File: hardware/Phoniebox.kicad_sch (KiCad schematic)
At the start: 11 parts, among them J1 GPIO, J2 Screw_Terminal_01x08, J3 Screw_Terminal_01x08, J4 Screw_Terminal_01x08, J5 Conn_02x02_Odd_Even, J7 USB_C_Receptacle_USB2.0, J8 Conn_02x04_Odd_Even, U4 CAT24C32

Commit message: Smaller high value caps. Standard R/C footprints instead of hand solder.
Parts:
- R1, R2, R30: footprint Resistor_SMD:R_0603_1608Metric_Pad0.98x0.95mm_HandSolder -> Resistor_SMD:R_0603_1608Metric

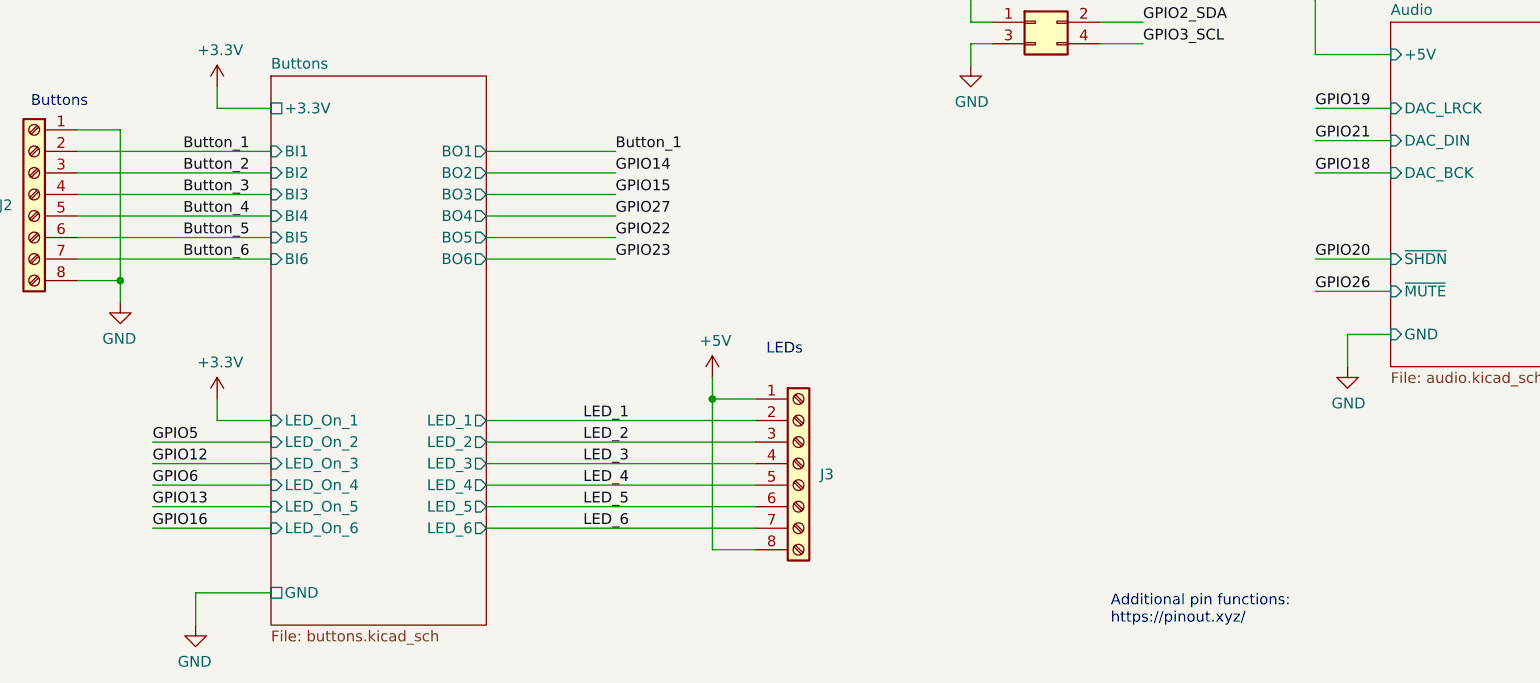
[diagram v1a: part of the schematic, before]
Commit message: Move a lot of parts. Switch audio l/r (only in schematic). Next step: Apply in PCB.
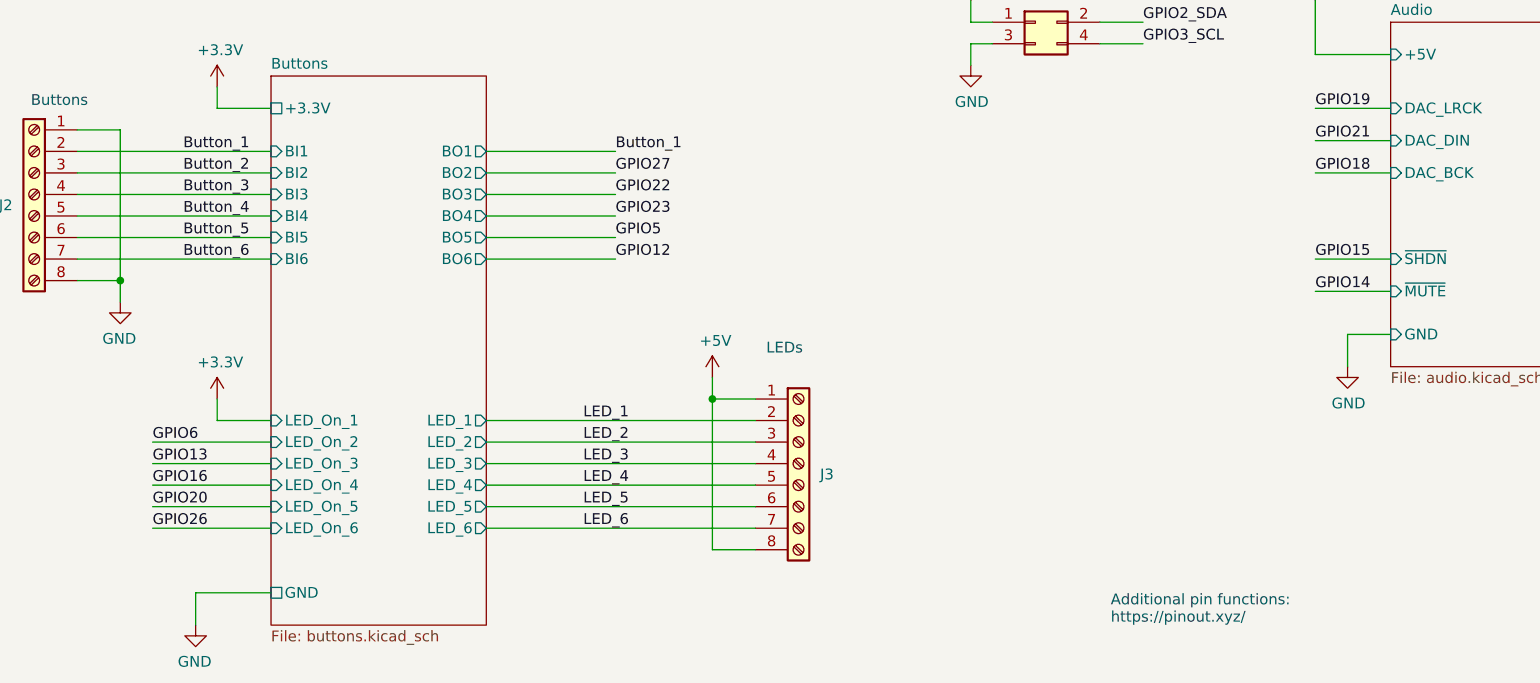
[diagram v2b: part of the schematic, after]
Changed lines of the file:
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@@
     (effects (font (size 1.27 1.27)) (justify left bottom))
   )
-  (label "GPIO23" (at 120.65 137.16 0)
+  (label "GPIO12" (at 120.65 137.16 0)
     (effects (font (size 1.27 1.27)) (justify left bottom))
   )
@@
     (effects (font (size 1.27 1.27)) (justify left bottom))
   )
-  (label "GPIO20" (at 203.2 137.16 0)
+  (label "GPIO15" (at 203.2 137.16 0)
     (effects (font (size 1.27 1.27)) (justify left bottom))
   )
@@
     (effects (font (size 1.27 1.27)) (justify right bottom))
   )
-  (label "GPIO13" (at 66.04 166.37 0)
+  (label "GPIO20" (at 66.04 166.37 0)
     (effects (font (size 1.27 1.27)) (justify left bottom))
   )
@@
     (effects (font (size 1.27 1.27)) (justify right bottom))
   )
-  (label "GPIO16" (at 66.04 168.91 0)
+  (label "GPIO26" (at 66.04 168.91 0)
     (effects (font (size 1.27 1.27)) (justify left bottom))
   )
@@
     (effects (font (size 1.27 1.27)) (justify right bottom))
   )
-  (label "GPIO22" (at 120.65 134.62 0)
-    (effects (font (size 1.27 1.27)) (justify left bottom))
-  )
-  (label "GPIO14" (at 120.65 127 0)
-    (effects (font (size 1.27 1.27)) (justify left bottom))
-  )
-  (label "GPIO12" (at 66.04 161.29 0)
-    (effects (font (size 1.27 1.27)) (justify left bottom))
-  )
-  (label "GPIO5" (at 66.04 158.75 0)
-    (effects (font (size 1.27 1.27)) (justify left bottom))
-  )
-  (label "GPIO27" (at 120.65 132.08 0)
-    (effects (font (size 1.27 1.27)) (justify left bottom))
-  )
-  (label "GPIO6" (at 66.04 163.83 0)
-    (effects (font (size 1.27 1.27)) (justify left bottom))
-  )
-  (label "GPIO26" (at 203.2 140.97 0)
+  (label "GPIO5" (at 120.65 134.62 0)
+    (effects (font (size 1.27 1.27)) (justify left bottom))
+  )
+  (label "GPIO27" (at 120.65 127 0)
+    (effects (font (size 1.27 1.27)) (justify left bottom))
+  )
+  (label "GPIO13" (at 66.04 161.29 0)
+    (effects (font (size 1.27 1.27)) (justify left bottom))
+  )
+  (label "GPIO6" (at 66.04 158.75 0)
+    (effects (font (size 1.27 1.27)) (justify left bottom))
+  )
+  (label "GPIO23" (at 120.65 132.08 0)
+    (effects (font (size 1.27 1.27)) (justify left bottom))
+  )
+  (label "GPIO16" (at 66.04 163.83 0)
+    (effects (font (size 1.27 1.27)) (justify left bottom))
+  )
+  (label "GPIO14" (at 203.2 140.97 0)
     (effects (font (size 1.27 1.27)) (justify left bottom))
   )
@@
     (effects (font (size 1.27 1.27)) (justify left bottom))
   )
-  (label "GPIO15" (at 120.65 129.54 0)
-    (effects (font (size 1.27 1.27)) (justify left bottom))
-  )
+  (label "GPIO22" (at 120.65 129.54 0)
+    (effects (font (size 1.27 1.27)) (justify left bottom))
+  )

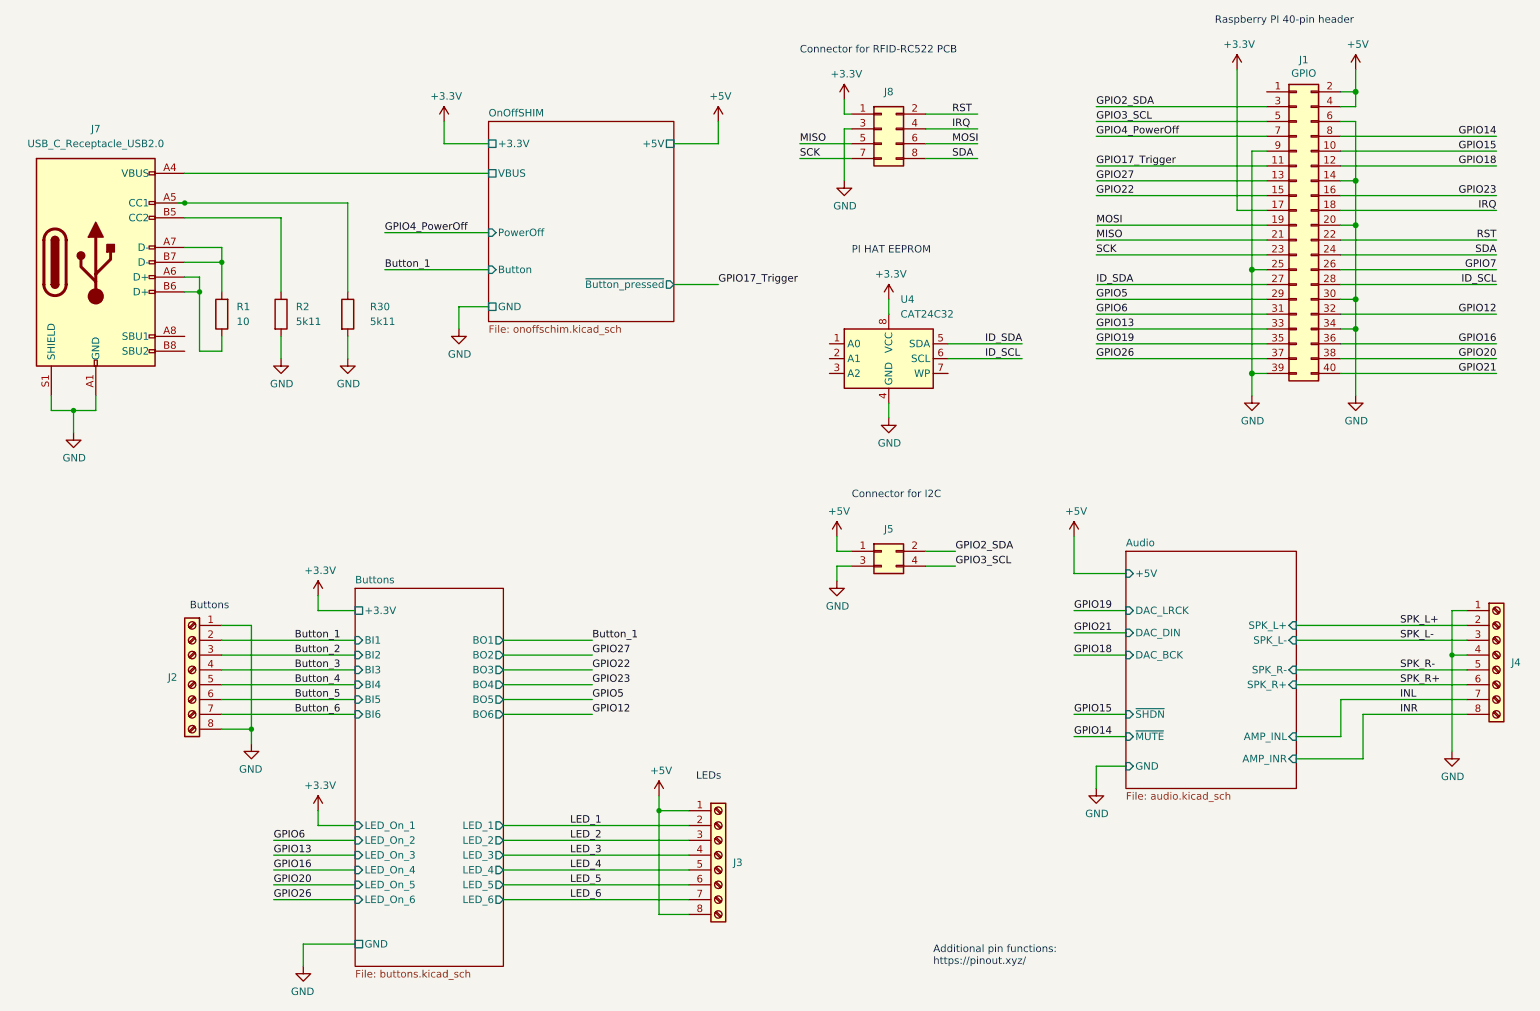
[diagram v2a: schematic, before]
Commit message: Moved DAC. Replace pin headers with single row SMD ones (compatible with RC522/display PCBs to connect).
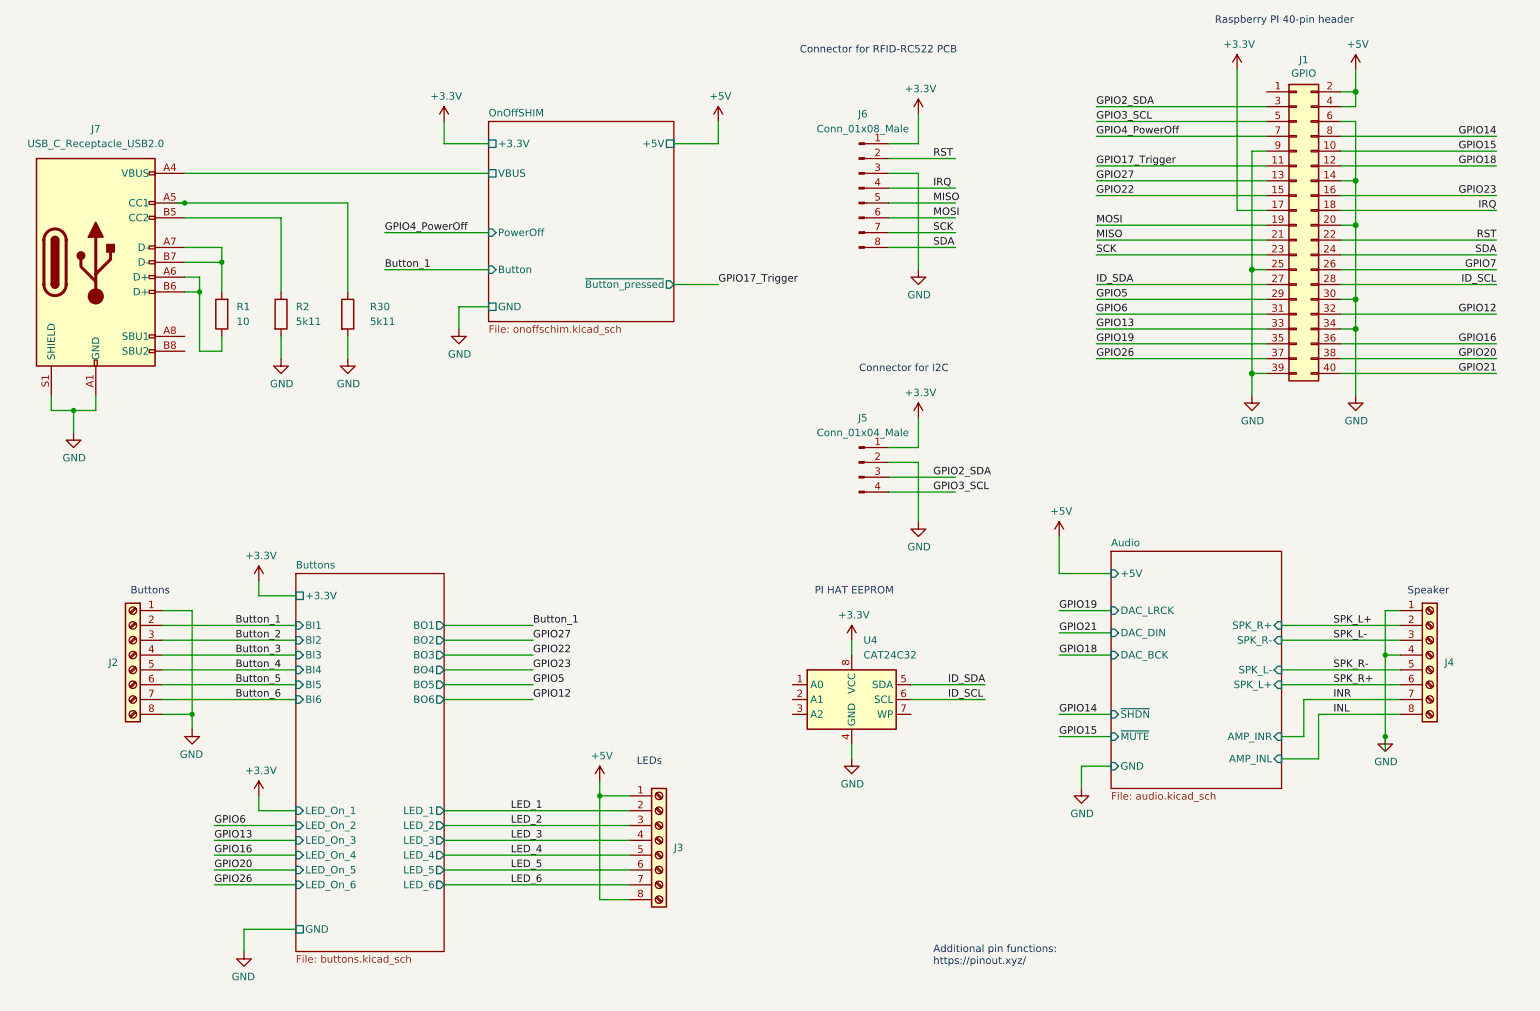
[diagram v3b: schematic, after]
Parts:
- removed J5: Conn_02x02_Odd_Even, Connector_PinHeader_2.54mm:PinHeader_2x02_P2.54mm_Vertical_SMD, symbol Connector_Generic:Conn_02x02_Odd_Even
- removed J8: Conn_02x04_Odd_Even, Connector_PinHeader_2.54mm:PinHeader_2x04_P2.54mm_Vertical_SMD, symbol Connector_Generic:Conn_02x04_Odd_Even
- added J5: Conn_01x04_Male, Connector_PinHeader_2.54mm:PinHeader_1x04_P2.54mm_Vertical_SMD_Pin1Left, symbol Connector:Conn_01x04_Male
- added J6: Conn_01x08_Male, Connector_PinHeader_2.54mm:PinHeader_1x08_P2.54mm_Vertical_SMD_Pin1Left, symbol Connector:Conn_01x08_Male
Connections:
- net +3V3: now also J5.1 (Pin_1), J6.1 (Pin_1)
- net GND: now also J5.2 (Pin_2), J6.3 (Pin_3)
- net GPIO2_SDA: now also J5.3 (Pin_3)
- net GPIO3_SCL: now also J5.4 (Pin_4)
- net INL: now also J4.8 (Pin_8); no longer J4.7 (Pin_7)
- net INR: now also J4.7 (Pin_7); no longer J4.8 (Pin_8)
- net IRQ: now also J6.4 (Pin_4)
- net MISO: now also J6.5 (Pin_5)
- net MOSI: now also J6.6 (Pin_6)
- net RST: now also J6.2 (Pin_2)
- net SCK: now also J6.7 (Pin_7)
- net SDA: now also J6.8 (Pin_8)
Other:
- note added: "Speaker"
- moved on the sheet: J2, J3, J4, U4

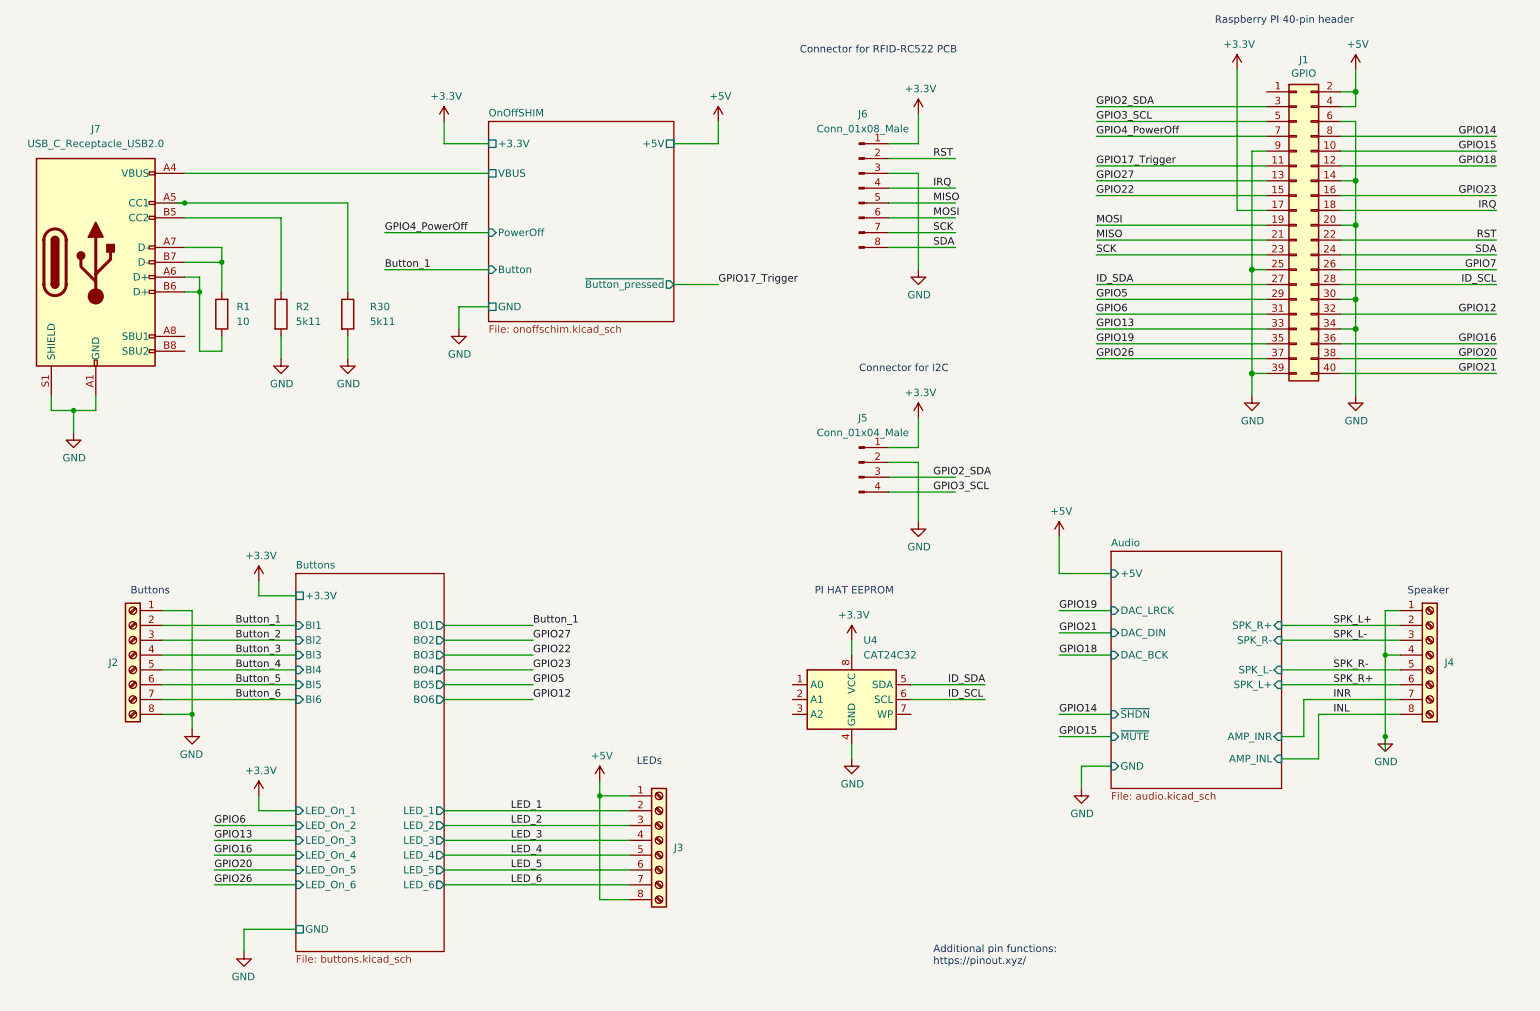
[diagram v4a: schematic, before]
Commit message: Fix all ERC warnings. Replace 4u7 capacitor in cut-off circuit by 100 nF cap and 10 kOhm in series to reduce stress on Raspi GPIO.
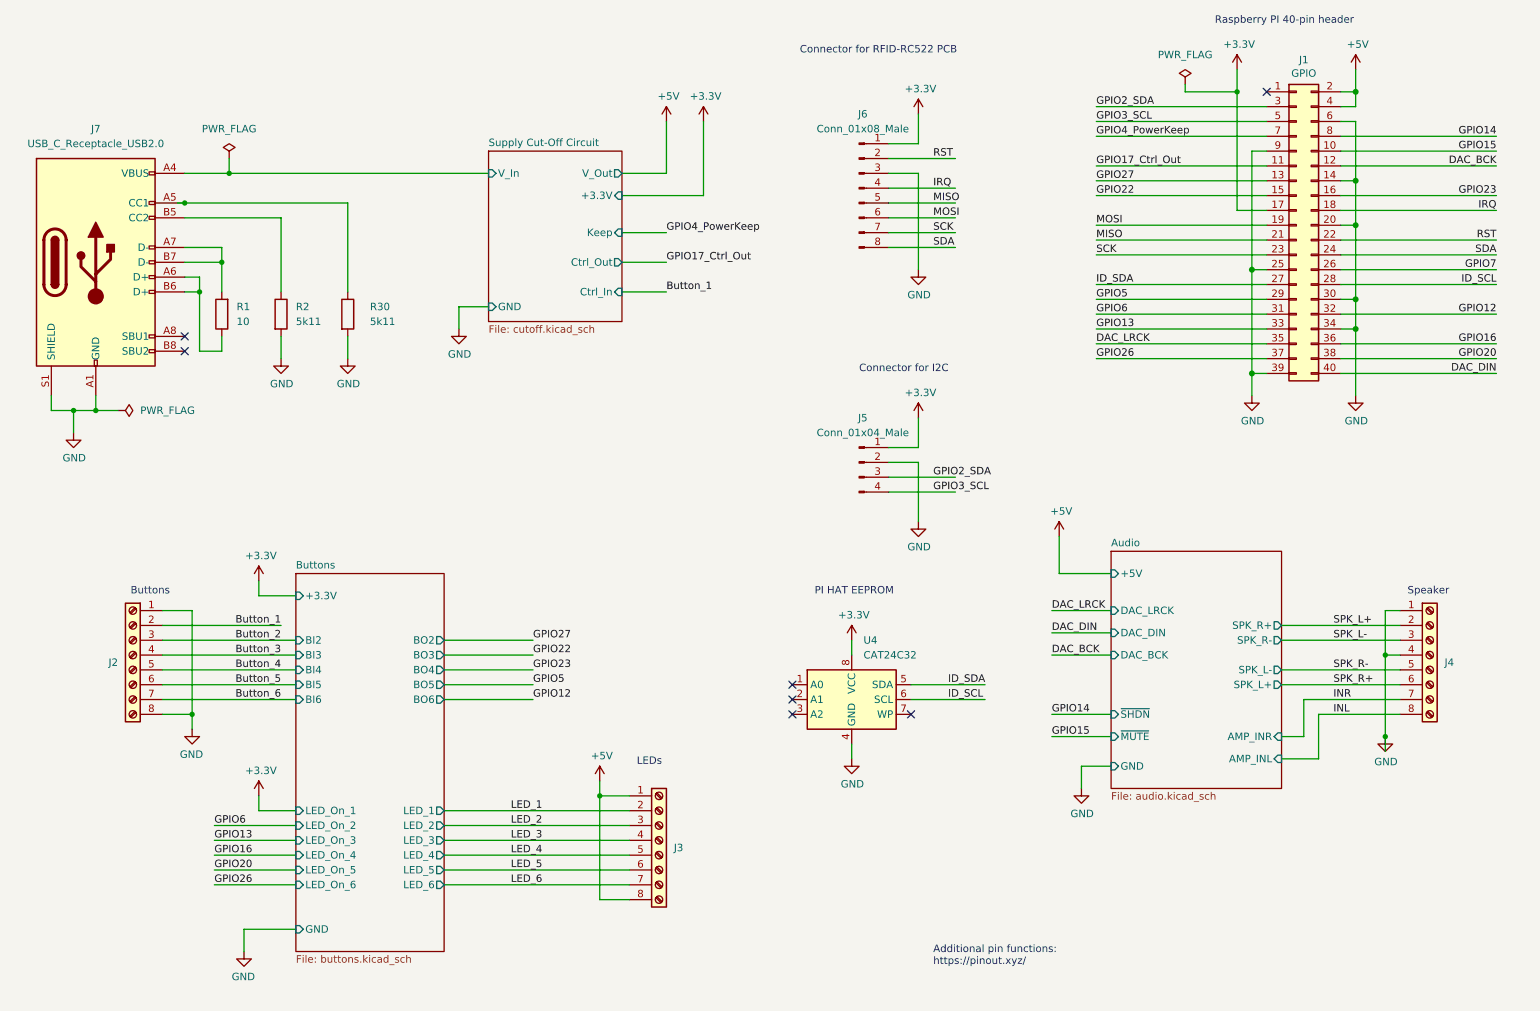
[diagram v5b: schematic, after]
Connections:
- net +3V3 renamed +3.3V
- net GPIO17_Trigger renamed GPIO17_Ctrl_Out
- net GPIO18 renamed DAC_BCK
- net GPIO19 renamed DAC_LRCK
- net GPIO21 renamed DAC_DIN
- net GPIO4_PowerOff renamed GPIO4_PowerKeep
- net Supply Cut-Off Circuit/VBUS renamed Supply Cut-Off Circuit/V_In
- no-connect marks 0 -> 7
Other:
- sheet OnOffSHIM renamed Supply Cut-Off Circuit
- sheet Buttons ports: added none; removed BI1, BO1
- sheet Supply Cut-Off Circuit: file onoffschim.kicad_sch -> cutoff.kicad_sch
- sheet Supply Cut-Off Circuit ports: added Ctrl_In, Ctrl_Out, Keep, V_In, V_Out; removed +5V, Button, PowerOff, VBUS, ~{Button_pressed}
